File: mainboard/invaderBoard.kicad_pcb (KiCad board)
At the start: 2 copper layers, 12.7 x 2.5 mm, 35 parts, among them J1 Conn_01x02, J10 Conn_01x04, J11 Conn_01x04, J12 Conn_01x04, J13 Conn_01x03, J14 Conn_01x04, J15 Conn_01x04, J16 Conn_01x04, J17 Conn_01x04, J18 Conn_01x04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

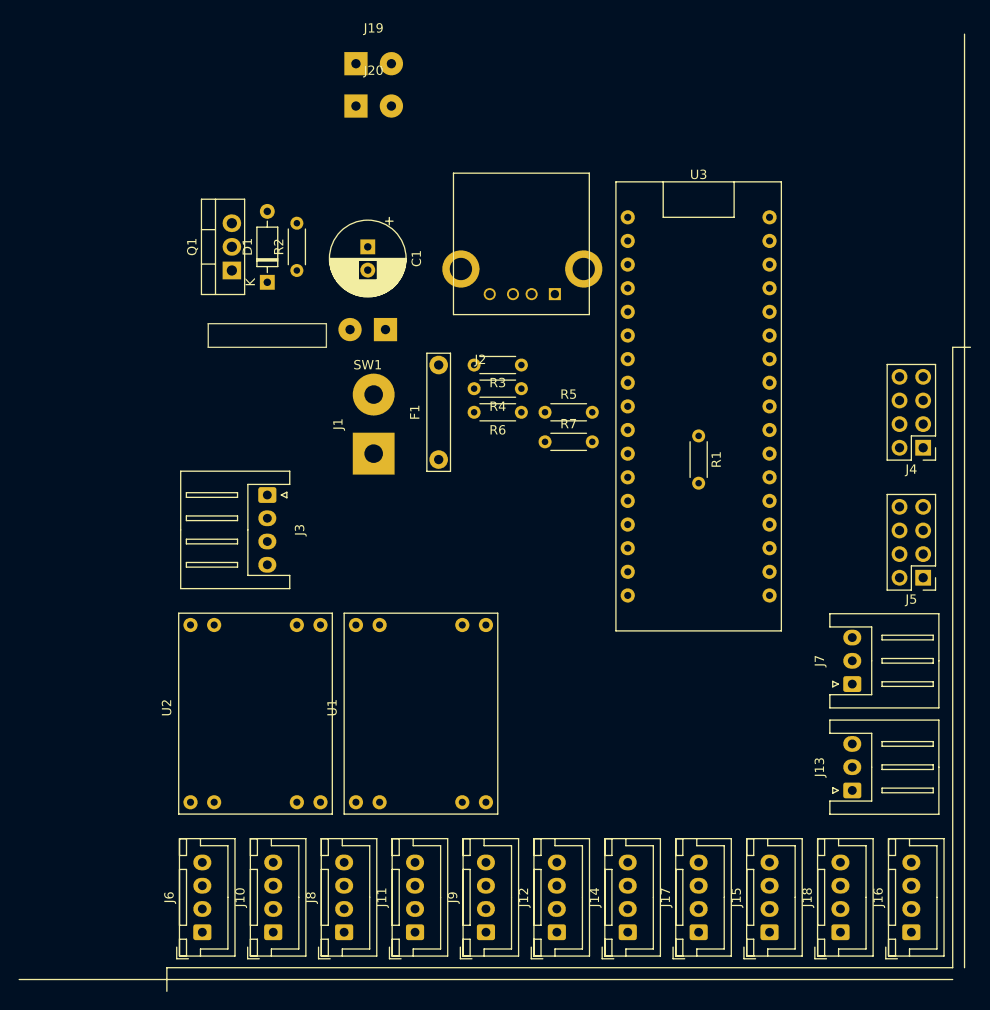
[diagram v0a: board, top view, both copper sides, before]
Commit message: Updated PCB - layout done, routing isn't
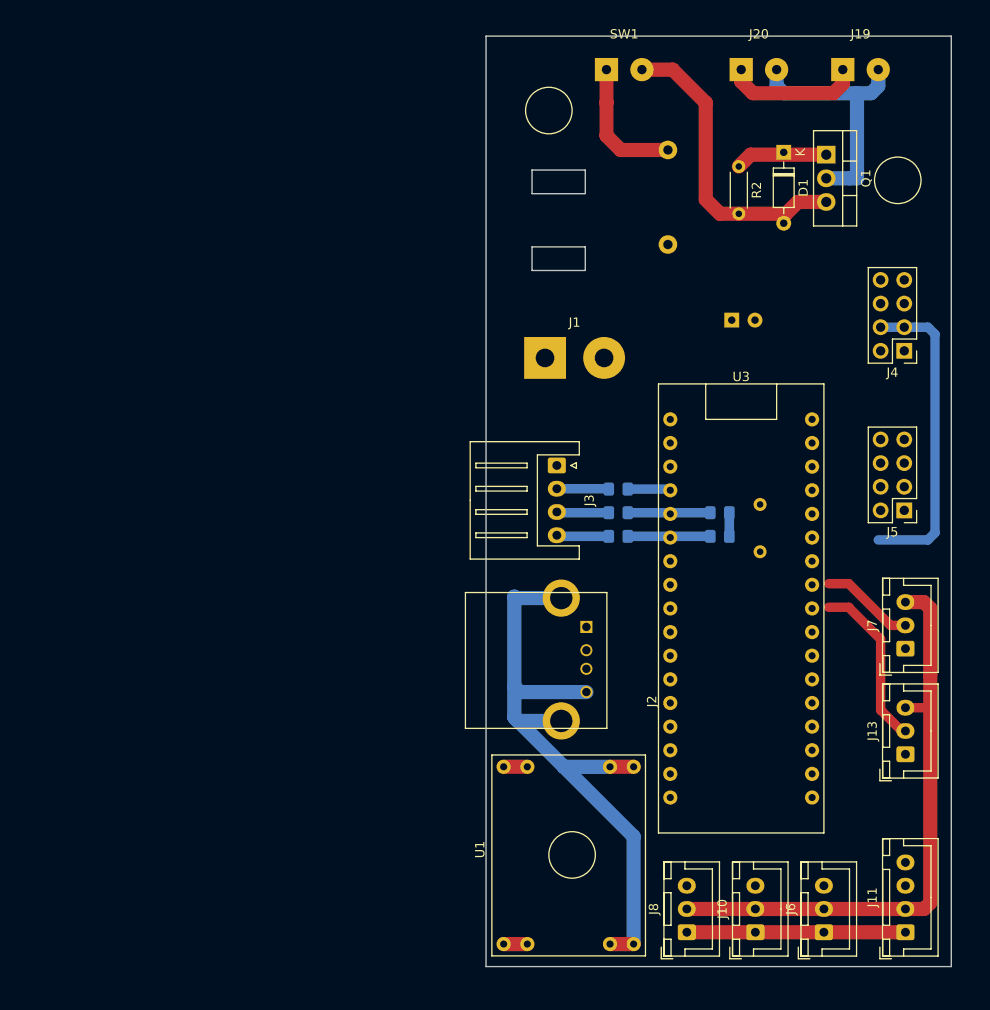
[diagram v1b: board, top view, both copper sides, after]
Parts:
- removed J12, J14, J15, J16, J17, J18, J9: Conn_01x04, Connector_JST:JST_XH_B4B-XH-A_1x04_P2.50mm_Vertical
- removed U2: LM2596, bluerSaab:LM2596
- C1, F1, R1: moved to B.Cu
- J10, J6, J8: value Conn_01x04 -> Conn_01x03; footprint Connector_JST:JST_XH_B4B-XH-A_1x04_P2.50mm_Vertical -> Connector_JST:JST_XH_B3B-XH-A_1x03_P2.50mm_Vertical
- J13, J7: footprint Connector_JST:JST_XH_S3B-XH-A_1x03_P2.50mm_Horizontal -> Connector_JST:JST_XH_B3B-XH-A_1x03_P2.50mm_Vertical
- R3, R4, R5, R6, R7: footprint Resistor_THT:R_Axial_DIN0204_L3.6mm_D1.6mm_P5.08mm_Horizontal -> Resistor_SMD:R_0805_2012Metric_Pad1.15x1.40mm_HandSolder; moved to B.Cu
- moved J6 66.8 mm to (242.1, 130.8)
- moved Q1 65.1 mm to (242.3, 47.2), turned to 270 degrees
- moved D1 57.2 mm to (237.7, 47.0), turned to 270 degrees
- moved J11 52.7 mm to (250.8, 130.8)
- moved J19 52.3 mm to (244.1, 38.1)
- moved J10 51.8 mm to (234.7, 130.8)
- moved R2 48.8 mm to (232.9, 48.5), turned to 270 degrees
- moved J20 41.6 mm to (233.2, 38.1)
- moved J2 40.0 mm to (216.5, 101.6), turned to 270 degrees
- moved C1 39.9 mm to (232.2, 65.0), turned to 0 degrees
- moved J8 36.8 mm to (227.3, 130.8)
- moved SW1 36.7 mm to (218.7, 38.1), turned to 0 degrees
- moved F1 33.8 mm to (225.3, 46.7)
- moved J3 31.3 mm to (213.4, 80.6)
- moved U3 22.2 mm to (233.2, 85.9)
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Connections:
- J10 pad 3: /AUX_POWER -> /USER_A4
- J11 pad 3: /AUX_POWER -> /USER_RX
- J11 pad 4: /USER_MISO -> /USER_TX
- J2 pad 2: Net-(J2-Pad2) -> (no net)
- J2 pad 3: Net-(J2-Pad3) -> (no net)
- J3 pad 1: Net-(J3-Pad1) -> (no net)
- J4 pad 5: Net-(J4-Pad5) -> (no net)
- J4 pad 6: Net-(J4-Pad6) -> (no net)
- J5 pad 5: Net-(J5-Pad5) -> (no net)
- J5 pad 6: Net-(J5-Pad6) -> (no net)
- J6 pad 3: /AUX_POWER -> /USER_A3
- J8 pad 3: /AUX_POWER -> /USER_A5
- U3 pad 1: Net-(U3-Pad1) -> (no net)
- U3 pad 10: Net-(U3-Pad10) -> (no net)
- U3 pad 11: Net-(U3-Pad11) -> (no net)
- U3 pad 12: Net-(U3-Pad12) -> (no net)
- U3 pad 13: Net-(U3-Pad13) -> (no net)
- U3 pad 16: /USER_MISO -> (no net)
- U3 pad 17: /USER_SCK -> (no net)
- U3 pad 18: /USER_MOSI -> (no net)
- U3 pad 19: /USER_SS -> (no net)
- U3 pad 2: Net-(U3-Pad2) -> (no net)
- U3 pad 22: Net-(U3-Pad22) -> (no net)
- U3 pad 24: /USER_SDA -> (no net)
- U3 pad 25: /USER_SCL -> (no net)
- U3 pad 3: Net-(U3-Pad3) -> (no net)
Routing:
- net /GND: track 0.00 -> 196.4 mm
- net /HV: track 0.00 -> 43.2 mm
- net /BATT_GND: track 0.00 -> 36.1 mm
- net /M1_DIR: track 0.00 -> 33.9 mm
- net Net-(C1-Pad2): track 0.00 -> 19.7 mm
- net /LIGHT_DIN_1: track 0.00 -> 18.2 mm
- net Net-(F1-Pad1): track 0.00 -> 14.3 mm
- net /LIGHT_DIN_2: track 0.00 -> 10.1 mm
- net /CELL_2: track 0.00 -> 8.97 mm
- net /CELL_3: track 0.00 -> 8.97 mm
- net /BATT_CELL_3: track 0.00 -> 5.63 mm
- net /BATT_CELL_2: track 0.00 -> 5.61 mm
- net /BATT_CELL_1: track 0.00 -> 5.60 mm
- net /CELL_1: track 0.00 -> 4.62 mm
- net /5V: track 0.00 -> 2.54 mm
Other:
- board size 12.7 x 2.5 mm -> 50 x 100 mm

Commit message: PCB Done, some changes on schematics
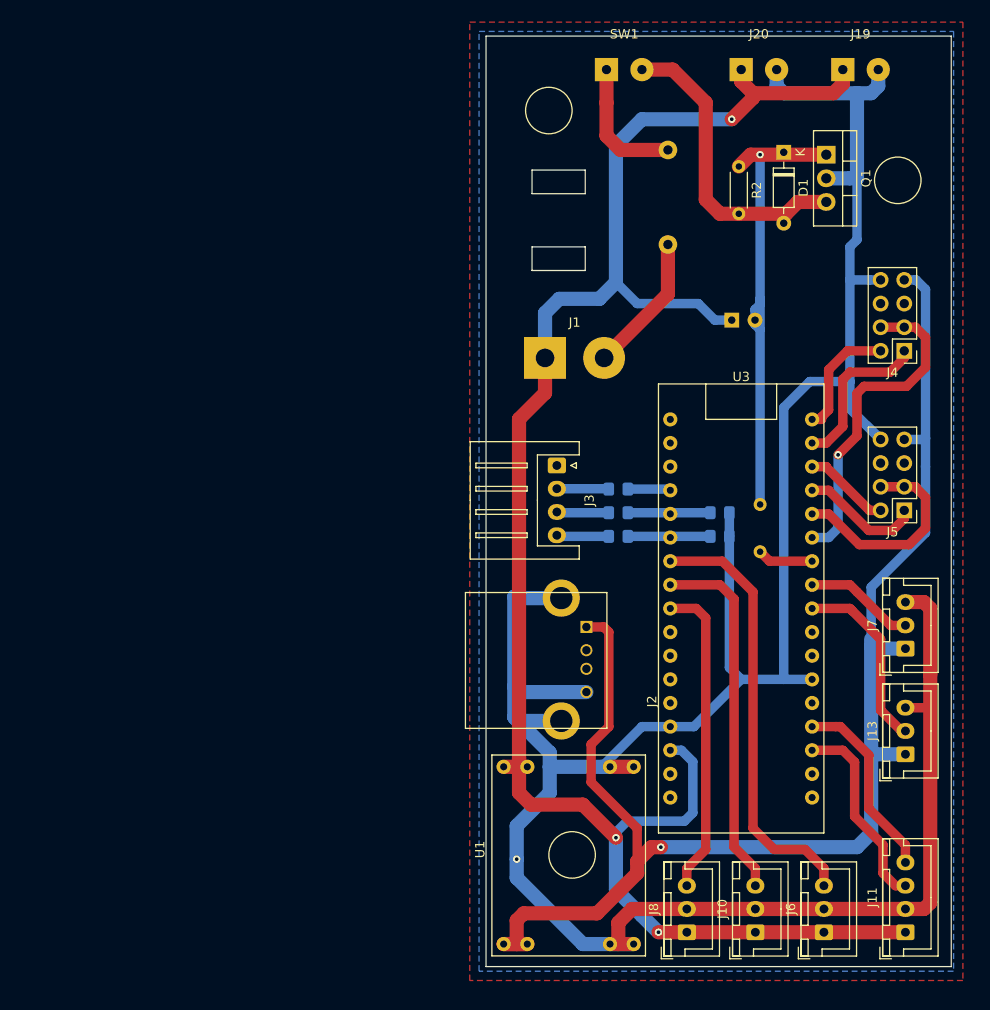
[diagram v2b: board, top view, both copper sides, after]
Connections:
- J11 pad 3: /USER_RX -> /USER_TX
- J11 pad 4: /USER_TX -> /USER_RX
- U3 pad 29: /M2_DIR -> /M1_DIR
- U3 pad 30: /M1_DIR -> /M2_DIR
- U3 pad 31: /M2_LPWM -> /M2_RPWM
- U3 pad 32: /M2_RPWM -> /M2_LPWM
- U3 pad 33: /M1_LPWM -> /M1_RPWM
- U3 pad 34: /M1_RPWM -> /M1_LPWM
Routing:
- net /HV: track 43.2 -> 197.9 mm, vias 0 -> 3
- net /5V: track 2.54 -> 153.9 mm, vias 0 -> 1
- net /GND: track 196.4 -> 330.3 mm, vias 0 -> 1
- net /USER_A3: track 0.00 -> 46.9 mm
- net Net-(C1-Pad2): track 19.7 -> 61.0 mm, vias 0 -> 1
- net /USER_A4: track 0.00 -> 39.3 mm
- net /USER_A5: track 0.00 -> 33.9 mm
- net /M2_DIR: track 0.00 -> 22.9 mm
- net /USER_TX: track 0.00 -> 21.3 mm
- net /USER_RX: track 0.00 -> 20.5 mm
- net /M1_RPWM: track 0.00 -> 17.4 mm
- net Net-(F1-Pad2): track 0.00 -> 15.0 mm
- net /M2_RPWM: track 0.00 -> 13.1 mm
- net /M1_LPWM: track 0.00 -> 13.1 mm
- net /M2_LPWM: track 0.00 -> 9.35 mm
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- added copper zone on B.Cu, net /GND
- added copper zone on F.Cu, net /GND

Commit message: PCB holes added + capacitor simulator in LTspice
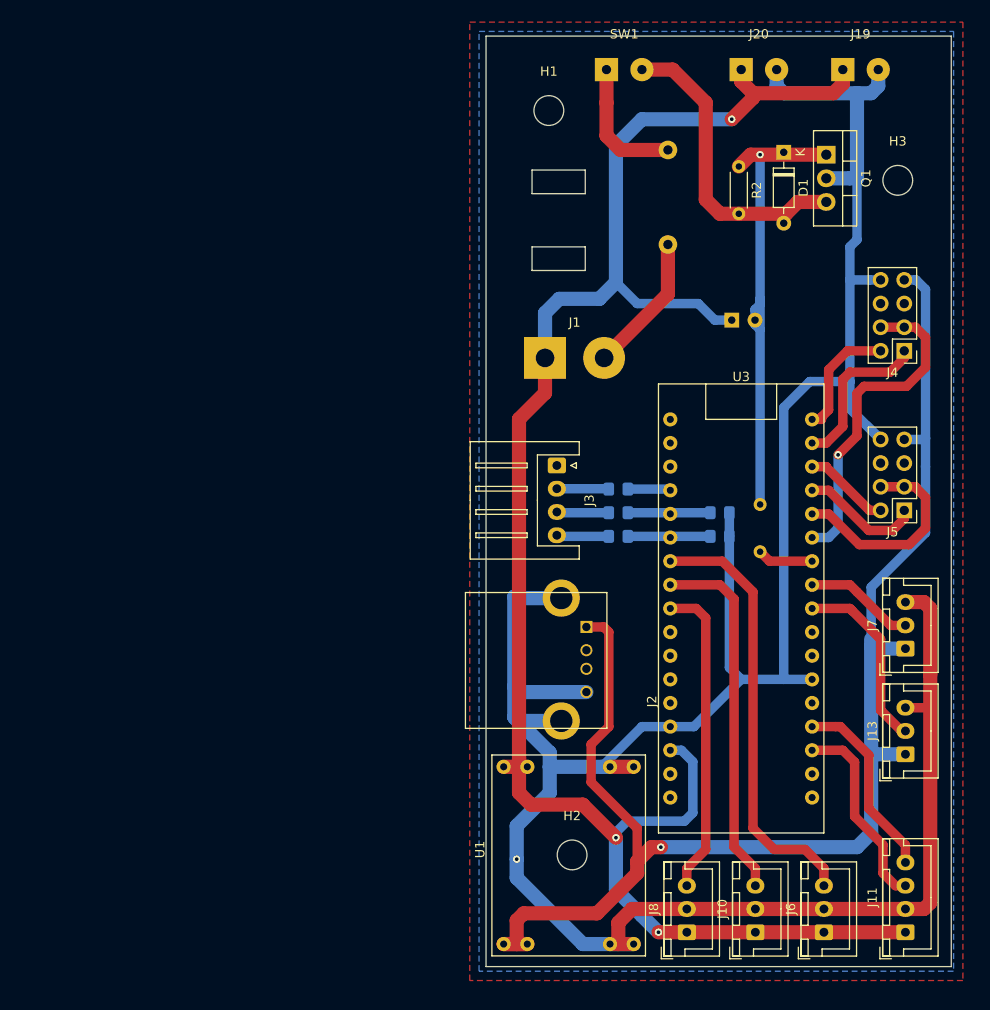
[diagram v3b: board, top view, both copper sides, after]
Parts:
- added H1: MountingHole, MountingHole:MountingHole_3.2mm_M3, F.Cu at (212.5, 42.5)
- added H2: MountingHole, MountingHole:MountingHole_3.2mm_M3, F.Cu at (215.0, 122.5)
- added H3: MountingHole, MountingHole:MountingHole_3.2mm_M3, F.Cu at (250.0, 50.0)
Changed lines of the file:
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@@
-(kicad_pcb (version 20171130) (host pcbnew "(5.1.2)-2")
+(kicad_pcb (version 20171130) (host pcbnew "(5.1.2)-1")
   (general
     (thickness 1.6)
-    (drawings 15)
+    (drawings 12)
     (tracks 292)
     (zones 0)
-    (modules 27)
+    (modules 30)
     (nets 28)
   )
@@
   )
   (setup
-    (last_trace_width 1.016)
+    (last_trace_width 0.25)
     (user_trace_width 0.508)
     (user_trace_width 1.016)
@@
     (add_net "Net-(F1-Pad1)")
     (add_net "Net-(F1-Pad2)")
+  )
+  (module MountingHole:MountingHole_3.2mm_M3 (layer F.Cu)
+    (at 250 50)
+    (descr "Mounting Hole 3.2mm, no annular, M3")
+    (tags "mounting hole 3.2mm no annular m3")
+    (attr virtual)
+    (fp_text reference H3 (at 0 -4.2) (layer F.SilkS)
+      (effects (font (size 1 1) (thickness 0.15)))
+    )
+    (fp_text value MountingHole (at 0 4.2) (layer F.Fab)
+      (effects (font (size 1 1) (thickness 0.15)))
+    )
+    (fp_circle (center 0 0) (end 3.45 0) (layer F.CrtYd) (width 0.05))
+    (fp_circle (center 0 0) (end 3.2 0) (layer Cmts.User) (width 0.15))
+    (fp_text user %R (at 0.3 0) (layer F.Fab)
+      (effects (font (size 1 1) (thickness 0.15)))
+    )
+    (pad 1 np_thru_hole circle (at 0 0) (size 3.2 3.2) (drill 3.2) (layers *.Cu *.Mask))
+  )
+  (module MountingHole:MountingHole_3.2mm_M3 (layer F.Cu)
+    (at 215 122.5)
+    (descr "Mounting Hole 3.2mm, no annular, M3")
+    (tags "mounting hole 3.2mm no annular m3")
+    (attr virtual)
+    (fp_text reference H2 (at 0 -4.2) (layer F.SilkS)
+      (effects (font (size 1 1) (thickness 0.15)))
+    )
+    (fp_text value MountingHole (at 0 4.2) (layer F.Fab)
+      (effects (font (size 1 1) (thickness 0.15)))
+    )
+    (fp_circle (center 0 0) (end 3.45 0) (layer F.CrtYd) (width 0.05))
+    (fp_circle (center 0 0) (end 3.2 0) (layer Cmts.User) (width 0.15))
+    (fp_text user %R (at 0.3 0) (layer F.Fab)
+      (effects (font (size 1 1) (thickness 0.15)))
+    )
+    (pad 1 np_thru_hole circle (at 0 0) (size 3.2 3.2) (drill 3.2) (layers *.Cu *.Mask))
+  )
+  (module MountingHole:MountingHole_3.2mm_M3 (layer F.Cu)
+    (at 212.5 42.5)
+    (descr "Mounting Hole 3.2mm, no annular, M3")
+    (tags "mounting hole 3.2mm no annular m3")
+    (attr virtual)
+    (fp_text reference H1 (at 0 -4.2) (layer F.SilkS)
+      (effects (font (size 1 1) (thickness 0.15)))
+    )
+    (fp_text value MountingHole (at 0 4.2) (layer F.Fab)
+      (effects (font (size 1 1) (thickness 0.15)))
+    )
+    (fp_circle (center 0 0) (end 3.45 0) (layer F.CrtYd) (width 0.05))
+    (fp_circle (center 0 0) (end 3.2 0) (layer Cmts.User) (width 0.15))
+    (fp_text user %R (at 0.3 0) (layer F.Fab)
+      (effects (font (size 1 1) (thickness 0.15)))
+    )
+    (pad 1 np_thru_hole circle (at 0 0) (size 3.2 3.2) (drill 3.2) (layers *.Cu *.Mask))
   )
   (module "invaderBoard:Arduino Micro" (layer F.Cu)
@@
     )
   )
-  (gr_circle (center 250 50) (end 250 47.5) (layer F.SilkS) (width 0.12))
-  (gr_circle (center 212.5 42.5) (end 212.5 40) (layer F.SilkS) (width 0.12))
-  (gr_circle (center 215 122.5) (end 215 120) (layer F.SilkS) (width 0.12))
   (gr_line (start 205.75 134.5) (end 255.75 134.5) (layer Edge.Cuts) (width 0.05))
   (gr_line (start 205.75 34.5) (end 205.75 134.5) (layer Edge.Cuts) (width 0.05))
